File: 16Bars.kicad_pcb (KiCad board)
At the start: 2 copper layers, 30 x 69 mm, 5 parts, among them IC1 CD4033BE, IC2 CD4033BE, J1 CLOCK_IN

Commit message: LEDShield, Panel, Improve 16bars
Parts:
- added C1: 330uf, Capacitor_THT:CP_Axial_L18.0mm_D6.5mm_P25.00mm_Horizontal, F.Cu at (112.5, 90.5)
- added C2: 47uF, Capacitor_THT:CP_Axial_L18.0mm_D6.5mm_P25.00mm_Horizontal, F.Cu at (112.5, 98.6)
- added D1: 1N4001, Diode_THT:D_DO-15_P10.16mm_Horizontal, F.Cu at (112.5, 79.0)
- added D2: 1N4001, Diode_THT:D_DO-15_P10.16mm_Horizontal, F.Cu at (112.5, 73.8)
- added J2: Conn_02x05_Odd_Even, Connector_PinHeader_2.54mm:PinHeader_2x05_P2.54mm_Vertical, F.Cu at (141.8, 88.8)
- added L1: 220uH, Inductor_THT:L_Axial_L6.6mm_D2.7mm_P10.16mm_Horizontal_Vishay_IM-2, F.Cu at (112.1, 83.7)
- added L2: 220uH, Inductor_THT:L_Axial_L6.6mm_D2.7mm_P10.16mm_Horizontal_Vishay_IM-2, F.Cu at (126.2, 73.4)
- added R1: CLK_INHB_PD, Resistor_THT:R_Axial_DIN0204_L3.6mm_D1.6mm_P5.08mm_Horizontal, F.Cu at (72.0, 83.0)
- added R2: RESET_PD, Resistor_THT:R_Axial_DIN0204_L3.6mm_D1.6mm_P5.08mm_Horizontal, F.Cu at (76.5, 83.0)
- added R3: CLK_INHB_PD, Resistor_THT:R_Axial_DIN0204_L3.6mm_D1.6mm_P5.08mm_Horizontal, F.Cu at (60.0, 83.0)
- added R4: RESET_PD, Resistor_THT:R_Axial_DIN0204_L3.6mm_D1.6mm_P5.08mm_Horizontal, F.Cu at (64.0, 83.0)
- added SW1: RESET, Button_Switch_THT:SW_PUSH_6mm, F.Cu at (76.2, 132.2)
- moved J1 36.5 mm to (61.5, 137.8)
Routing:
- added copper zone on B.Cu, net GND
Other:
- board size 30 x 69 mm -> 30 x 105 mm

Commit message: Finished schematic and footprints
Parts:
- removed C1: 330uf, Capacitor_THT:CP_Axial_L18.0mm_D6.5mm_P25.00mm_Horizontal
- removed C2: 47uF, Capacitor_THT:CP_Axial_L18.0mm_D6.5mm_P25.00mm_Horizontal
- removed D1, D2: 1N4001, Diode_THT:D_DO-15_P10.16mm_Horizontal
- removed DS1, DS2: TDSR0760, SamacSys_Parts:TDSR0760
- removed IC1, IC2: CD4033BE, SamacSys_Parts:DIP794W53P254L1930H508Q16N
- removed J1: CLOCK_IN, Connector_Audio:Jack_3.5mm_QingPu_WQP-PJ398SM_Vertical_CircularHoles
- removed J2: Conn_02x05_Odd_Even, Connector_PinHeader_2.54mm:PinHeader_2x05_P2.54mm_Vertical
- removed L1, L2: 220uH, Inductor_THT:L_Axial_L6.6mm_D2.7mm_P10.16mm_Horizontal_Vishay_IM-2
- removed R1, R3: CLK_INHB_PD, Resistor_THT:R_Axial_DIN0204_L3.6mm_D1.6mm_P5.08mm_Horizontal
- removed R2, R4: RESET_PD, Resistor_THT:R_Axial_DIN0204_L3.6mm_D1.6mm_P5.08mm_Horizontal
- removed SW1: RESET, Button_Switch_THT:SW_PUSH_6mm

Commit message: Rough PCB Layout
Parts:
- added C1: 47uf, Capacitor_THT:C_Radial_D5.0mm_H11.0mm_P2.00mm, F.Cu at (71.0, 48.0)
- added C2: 100nf, Capacitor_THT:C_Disc_D7.0mm_W2.5mm_P5.00mm, F.Cu at (64.0, 75.0)
- added C3: 100nf, Capacitor_THT:C_Disc_D7.0mm_W2.5mm_P5.00mm, F.Cu at (59.5, 101.0)
- added C4: 100nf, Capacitor_THT:C_Disc_D7.0mm_W2.5mm_P5.00mm, F.Cu at (73.0, 101.0)
- added D1: 1N4148, Diode_THT:D_A-405_P7.62mm_Horizontal, F.Cu at (75.0, 55.2)
- added DS-ONES1: TDSR0760, SamacSys_Parts:TDSR0760, F.Cu at (81.0, 136.0)
- added DS-TENS1: TDSR0760, SamacSys_Parts:TDSR0760, F.Cu at (67.0, 136.0)
- added IC1: CD4033BE, SamacSys_Parts:DIP794W53P254L1930H508Q16N, F.Cu at (77.0, 113.0)
- added IC2: CD4033BE, SamacSys_Parts:DIP794W53P254L1930H508Q16N, F.Cu at (63.0, 113.0)
- added IC3: CD4510BE, SamacSys_Parts:DIP794W53P254L1930H508Q16N, F.Cu at (63.0, 87.0)
- added J1: CLOCK_IN, Connector_Audio:Jack_3.5mm_QingPu_WQP-PJ398SM_Vertical_CircularHoles, F.Cu at (62.0, 38.2)
- added J2: Conn_02x05_Odd_Even, Connector_PinHeader_2.54mm:PinHeader_2x05_P2.54mm_Vertical, F.Cu at (71.9, 41.3)
- added Q1: 2N3904, Package_TO_SOT_THT:TO-92_Inline, F.Cu at (60.0, 58.7)
- added Q2: 2N3904, Package_TO_SOT_THT:TO-92_Inline, F.Cu at (68.0, 58.7)
- added Q3: 2N3904, Package_TO_SOT_THT:TO-92_Inline, F.Cu at (60.0, 65.0)
- added Q4: 2N3904, Package_TO_SOT_THT:TO-92_Inline, F.Cu at (60.0, 71.0)
- added Q5: 2N3904, Package_TO_SOT_THT:TO-92_Inline, F.Cu at (68.0, 65.0)
- added Q6: 2N3904, Package_TO_SOT_THT:TO-92_Inline, F.Cu at (68.0, 70.7)
- added R1: CLK_INHB_PD, Resistor_THT:R_Axial_DIN0204_L3.6mm_D1.6mm_P5.08mm_Horizontal, F.Cu at (77.5, 66.0)
- added R10: R, Resistor_THT:R_Axial_DIN0204_L3.6mm_D1.6mm_P5.08mm_Horizontal, F.Cu at (69.5, 75.0)
- added R11: R, Resistor_THT:R_Axial_DIN0204_L3.6mm_D1.6mm_P5.08mm_Horizontal, F.Cu at (69.5, 79.2)
- added R12: R, Resistor_THT:R_Axial_DIN0204_L3.6mm_D1.6mm_P5.08mm_Horizontal, F.Cu at (69.5, 83.4)
- added R13: R, Resistor_THT:R_Axial_DIN0204_L3.6mm_D1.6mm_P5.08mm_Horizontal, F.Cu at (69.5, 87.6)
- added R14: R, Resistor_THT:R_Axial_DIN0204_L3.6mm_D1.6mm_P5.08mm_Horizontal, F.Cu at (69.5, 91.8)
- added R15: R, Resistor_THT:R_Axial_DIN0204_L3.6mm_D1.6mm_P5.08mm_Horizontal, F.Cu at (69.5, 96.0)
- added R2: RESET_PD, Resistor_THT:R_Axial_DIN0204_L3.6mm_D1.6mm_P5.08mm_Horizontal, F.Cu at (77.5, 69.4)
- added R3: 10K, Resistor_THT:R_Axial_DIN0204_L3.6mm_D1.6mm_P5.08mm_Horizontal, F.Cu at (77.5, 73.9)
- added R4: 10K, Resistor_THT:R_Axial_DIN0204_L3.6mm_D1.6mm_P5.08mm_Horizontal, F.Cu at (77.5, 78.3)
- added R5: 47K, Resistor_THT:R_Axial_DIN0204_L3.6mm_D1.6mm_P5.08mm_Horizontal, F.Cu at (58.5, 53.0)
- added R6: 10K, Resistor_THT:R_Axial_DIN0204_L3.6mm_D1.6mm_P5.08mm_Horizontal, F.Cu at (77.5, 82.7)
- added R7: 1K, Resistor_THT:R_Axial_DIN0204_L3.6mm_D1.6mm_P5.08mm_Horizontal, F.Cu at (77.5, 87.1)
- added R8: 10k, Resistor_THT:R_Axial_DIN0204_L3.6mm_D1.6mm_P5.08mm_Horizontal, F.Cu at (77.5, 91.6)
- added R9: 10K, Resistor_THT:R_Axial_DIN0204_L3.6mm_D1.6mm_P5.08mm_Horizontal, F.Cu at (77.5, 96.0)
- added SW1: RESET_CLOCK_LED, Button_Switch_THT:Thonk-LED-Button-MomentaryON, F.Cu at (77.4, 45.8)

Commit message: Update PCB layout, shrunk silkscreen size
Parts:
- moved J1 11.5 mm to (62.0, 49.8), turned to 180 degrees
- moved Q6 1.04 mm to (67.0, 71.0)
- moved Q2 1.00 mm to (67.0, 58.7)
- moved Q5 1.00 mm to (67.0, 65.0)
- moved C1 0.90 mm to (70.5, 47.2), turned to 90 degrees
- renumbered DS-ONES1 to DS-01S1, DS-TENS1 to DS-10S1

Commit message: PCB Layout Complete
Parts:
- added G***: LOGO, ArtworkFootprints:SixteenWinds, F.Cu at (83.0, 79.0)
- C1, C2, C3, C4, D1, IC1, IC2, IC3, J2, Q1, Q2, Q3, Q4, Q5, Q6, R1, R10, R11, R12, R13, R14, R15, R2, R3, R4, R5, R6, R7, R8, R9: moved to B.Cu
- moved R1 32.1 mm to (83.5, 97.5), turned to 180 degrees
- moved R8 30.7 mm to (74.5, 61.0), turned to 90 degrees
- moved R2 28.1 mm to (75.5, 97.5), turned to 180 degrees
- moved R7 26.1 mm to (78.0, 61.0), turned to 90 degrees
- moved R15 22.8 mm to (77.0, 74.5), turned to 180 degrees
- moved R3 21.2 mm to (78.5, 95.0)
- moved R4 16.8 mm to (75.5, 95.0), turned to 180 degrees
- moved R14 15.7 mm to (77.0, 78.0), turned to 180 degrees
- moved R5 15.5 mm to (74.0, 53.0), turned to 180 degrees
- moved R12 14.5 mm to (77.0, 71.0), turned to 180 degrees
- moved R11 13.9 mm to (77.0, 67.5), turned to 180 degrees
- moved R10 13.4 mm to (77.0, 64.0), turned to 180 degrees
- moved J1 12.5 mm to (62.0, 37.2), turned to 0 degrees
- moved R9 12.3 mm to (72.0, 85.0)
- moved R6 9.97 mm to (75.5, 92.5), turned to 180 degrees
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- renumbered DS-01S1 to DS-ONES1, DS-10S1 to DS-TENS1
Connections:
- net RESET renamed 16_BARS_RESET
- IC2 pad 14: GND -> unconnected-(IC2-Pad14)
- J1 pad S: (no net) -> GND
- J1 pad T: (no net) -> Net-(D1-Pad2)
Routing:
- net 16_BARS_RESET: track 0.00 -> 175.1 mm, vias 0 -> 1
- net /C1: track 0.00 -> 96.4 mm
- net /E1: track 0.00 -> 77.3 mm
- net /B2: track 0.00 -> 68.3 mm
- net CLOCK_BAR: track 0.00 -> 62.2 mm
- net GND: track 0.00 -> 57.2 mm, vias 0 -> 1
- net CLOCK_IN: track 0.00 -> 50.1 mm
- net /F2: track 0.00 -> 31.5 mm
- net /F1: track 0.00 -> 31.2 mm
- net /G2: track 0.00 -> 27.7 mm
- net /G1: track 0.00 -> 27.3 mm
- net Net-(Q5-Pad2): track 0.00 -> 27.1 mm
- net +12V: track 0.00 -> 26.9 mm, vias 0 -> 1
- net Net-(IC2-Pad2): track 0.00 -> 26.4 mm
- net Net-(Q2-Pad3): track 0.00 -> 25.5 mm
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- added copper zone on F.Cu, net +12V
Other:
- board size 30 x 105 mm -> 28.5 x 105 mm
- board text added: "16Bars Rev 0.0"

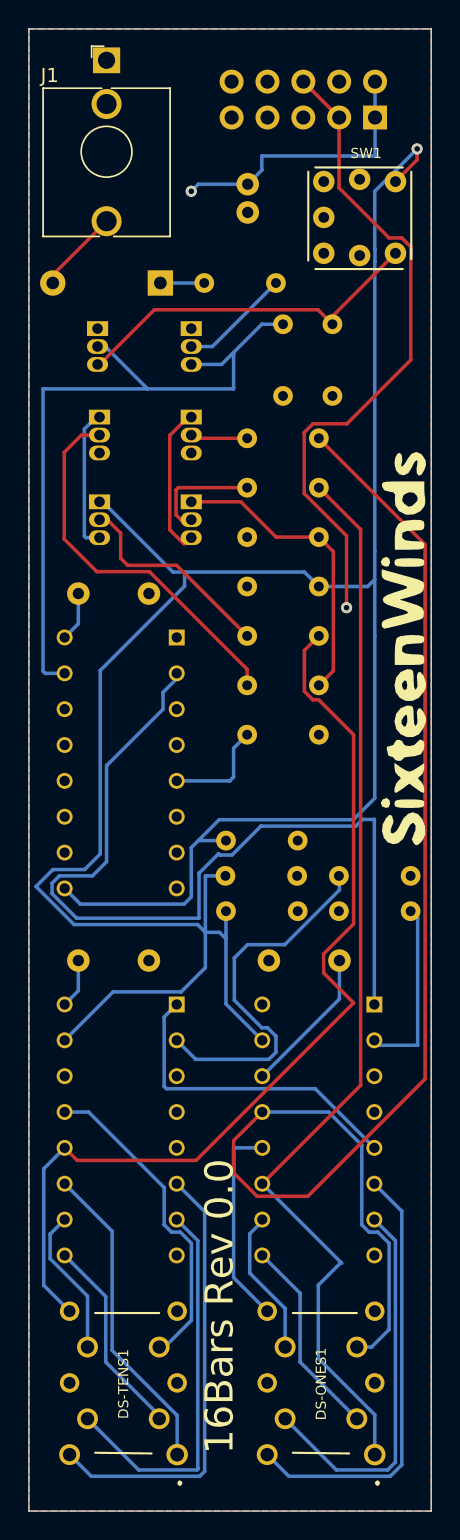
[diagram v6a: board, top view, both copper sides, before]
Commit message: Surface Mount Resistors and Caps, fix 7segment footprint
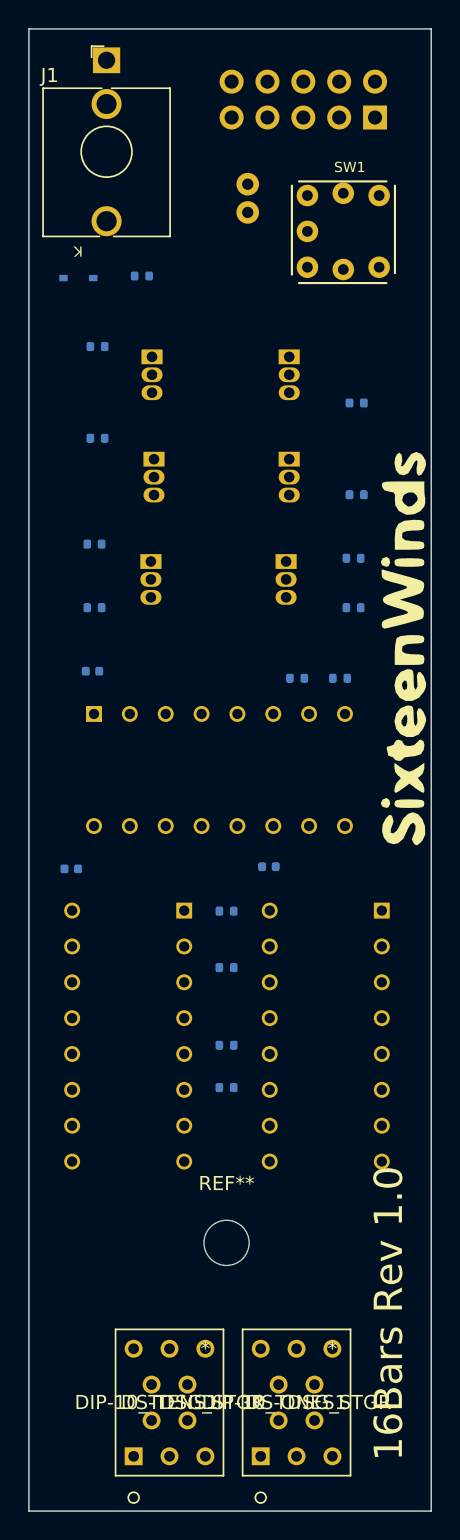
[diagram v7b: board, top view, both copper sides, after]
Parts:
- added REF**: MountingHole_3.2mm_M3, MountingHole:MountingHole_3.2mm_M3, F.Cu at (70.5, 121.0)
- C2, C3, C4: footprint Capacitor_THT:C_Disc_D7.0mm_W2.5mm_P5.00mm -> Capacitor_SMD:C_0402_1005Metric
- D1: footprint Diode_THT:D_A-405_P7.62mm_Horizontal -> Diode_SMD:D_SOD-323
- DS-ONES1, DS-TENS1: value TDSR0760 -> DIP-10_TDSG_STGR; footprint SamacSys_Parts:TDSR0760 -> TDSR*:TDSR0760
- R1, R10, R11, R12, R13, R14, R15, R2, R3, R4, R5, R6, R7, R8, R9: footprint Resistor_THT:R_Axial_DIN0204_L3.6mm_D1.6mm_P5.08mm_Horizontal -> Resistor_SMD:R_0402_1005Metric
- moved R13 23.5 mm to (61.4, 64.0)
- moved R1 18.1 mm to (70.5, 110.0)
- moved R14 17.2 mm to (61.1, 71.5)
- moved R7 17.0 mm to (61.4, 57.5), turned to 180 degrees
- moved R15 16.0 mm to (61.1, 76.0)
- moved R6 11.9 mm to (78.5, 81.0)
- moved R2 10.8 mm to (70.5, 107.0)
- moved R3 10.3 mm to (70.5, 101.5)
- moved R5 9.51 mm to (64.5, 52.5)
- moved C3 8.51 mm to (59.5, 94.5)
- moved C4 8.32 mm to (73.5, 94.3)
- moved DS-ONES1 8.08 mm to (78.0, 128.5), turned to 0 degrees
- moved Q4 7.94 mm to (74.7, 72.7)
- moved DS-TENS1 7.76 mm to (69.0, 128.5), turned to 0 degrees
- moved Q3 7.55 mm to (74.9, 65.5)
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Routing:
- net 16_BARS_RESET: track 175.1 -> 0.00 mm, vias 1 -> 0
- net /C1: track 96.4 -> 0.00 mm
- net /E1: track 77.3 -> 0.00 mm
- net /B2: track 68.3 -> 0.00 mm
- net CLOCK_BAR: track 62.2 -> 0.00 mm
- net GND: track 57.2 -> 0.00 mm, vias 1 -> 0
- net CLOCK_IN: track 50.1 -> 0.00 mm
- net /F2: track 31.5 -> 0.00 mm
- net /F1: track 31.2 -> 0.00 mm
- net /G2: track 27.7 -> 0.00 mm
- net /G1: track 27.3 -> 0.00 mm
- net Net-(Q5-Pad2): track 27.1 -> 0.00 mm
- net +12V: track 26.9 -> 0.00 mm, vias 1 -> 0
- net Net-(IC2-Pad2): track 26.4 -> 0.00 mm
- net Net-(Q2-Pad3): track 25.5 -> 0.00 mm
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- removed copper zone on F.Cu, net +12V
- removed copper zone on B.Cu, net GND
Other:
- board text added: "16Bars Rev 1.0"
- board text removed: "16Bars Rev 0.0"

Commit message: Tracks for 7Seg LEDs
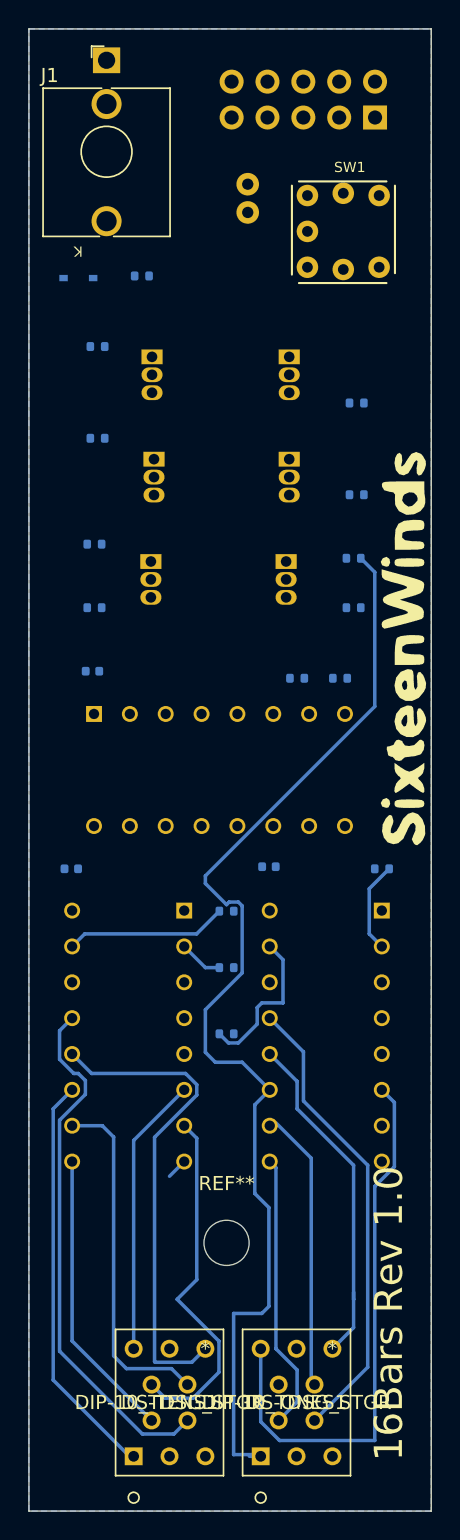
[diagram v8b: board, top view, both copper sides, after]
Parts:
- moved R1 19.0 mm to (81.5, 94.5)
- moved R2 0.81 mm to (70.5, 106.2)
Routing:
- net /E1: track 0.00 -> 80.8 mm
- net /F1: track 0.00 -> 39.6 mm
- net /C2: track 0.00 -> 37.6 mm
- net /B2: track 0.00 -> 34.6 mm
- net /C1: track 0.00 -> 32.9 mm
- net /E2: track 0.00 -> 29.1 mm
- net /G2: track 0.00 -> 25.6 mm
- net /A2: track 0.00 -> 24.8 mm
- net /B1: track 0.00 -> 24.5 mm
- net 16_BARS_RESET: track 0.00 -> 22.5 mm
- net /D2: track 0.00 -> 20.7 mm
- net /F2: track 0.00 -> 19.8 mm
- net /A1: track 0.00 -> 19.8 mm
- net /D1: track 0.00 -> 19.7 mm
- net Net-(IC1-Pad2): track 0.00 -> 6.45 mm
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- added copper zone on B.Cu, net GND
